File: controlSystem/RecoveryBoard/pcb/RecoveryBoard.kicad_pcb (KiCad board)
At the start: 2 copper layers, 102.7 x 56.8 mm, 150 parts, among them J1 Conn_01x06, J10 Conn_01x02, J11 Conn_01x03, J2 Thermistor, J3 Conn_01x04, J4 J-TE-Debug-2-1734592-0, J5 Conn_01x03, J6 Sensor Board 1, J7 Sensor Board 2, J8 Conn_01x06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

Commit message: Added rocket ready connector to ERS board
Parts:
- added J12: Conn_01x02, Connector_Molex:Molex_KK-254_AE-6410-02A_1x02_P2.54mm_Vertical, F.Cu at (119.8, 123.8)
- D8, D9: value D_Small -> SS210A
- moved TP24 5.53 mm to (122.1, 118.7)
- moved TP25 5.53 mm to (122.1, 116.9)
- moved TP26 2.90 mm to (122.1, 115.1)
- moved TP27 2.90 mm to (122.1, 113.3)
- moved TP8 2.90 mm to (122.1, 111.5)
- moved TP47 2.90 mm to (122.1, 109.7)
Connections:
- net Net-(TP41-Pad1) renamed /Microcontroller/ROCKET_READY
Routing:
- net /Microcontroller/USART2_TX: track 120.9 -> 243.6 mm, vias 2 -> 3
- net /Microcontroller/HALL2: track 119.6 -> 0.00 mm
- net /Microcontroller/ROCKET_READY: track 10.8 -> 22.6 mm
- net /Microcontroller/USART2_RX: track 114.7 -> 118.9 mm, vias 2 -> 3
- net BATT_READ: track 40.1 -> 43.4 mm
- net UMB_~{ON}: track 64.2 -> 66.5 mm
- net /Microcontroller/ISO_MAIN: track 16.8 -> 18.5 mm
- net MOTOR_ILIM: track 23.7 -> 22.7 mm
- net /Microcontroller/ISO_DROGUE: track 20.2 -> 21.3 mm
- net +3.3V: track 173.0 -> 172.3 mm
- net VBUS: vias 5 -> 0
- net GND: vias 56 -> 52
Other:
- board text added: "ROCKET READY"

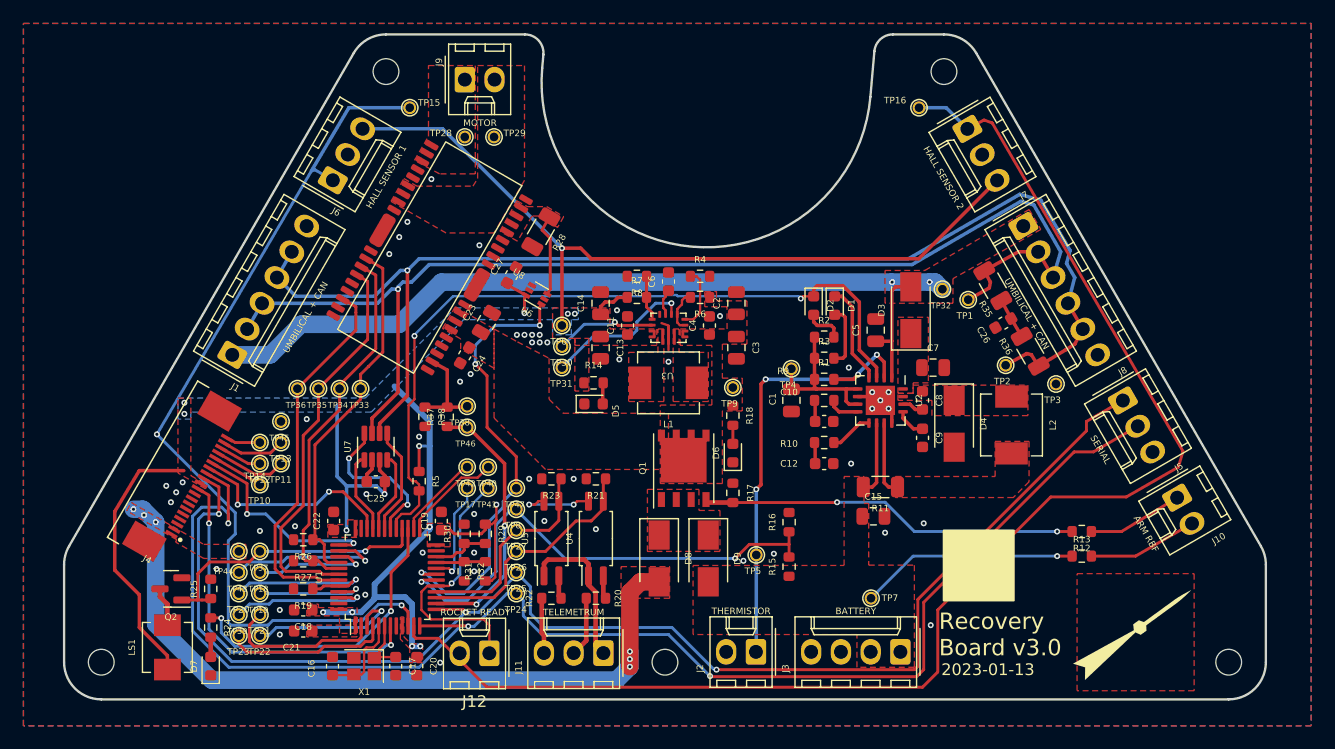
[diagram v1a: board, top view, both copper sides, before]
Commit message: Design review changes and cleaned up board layout.
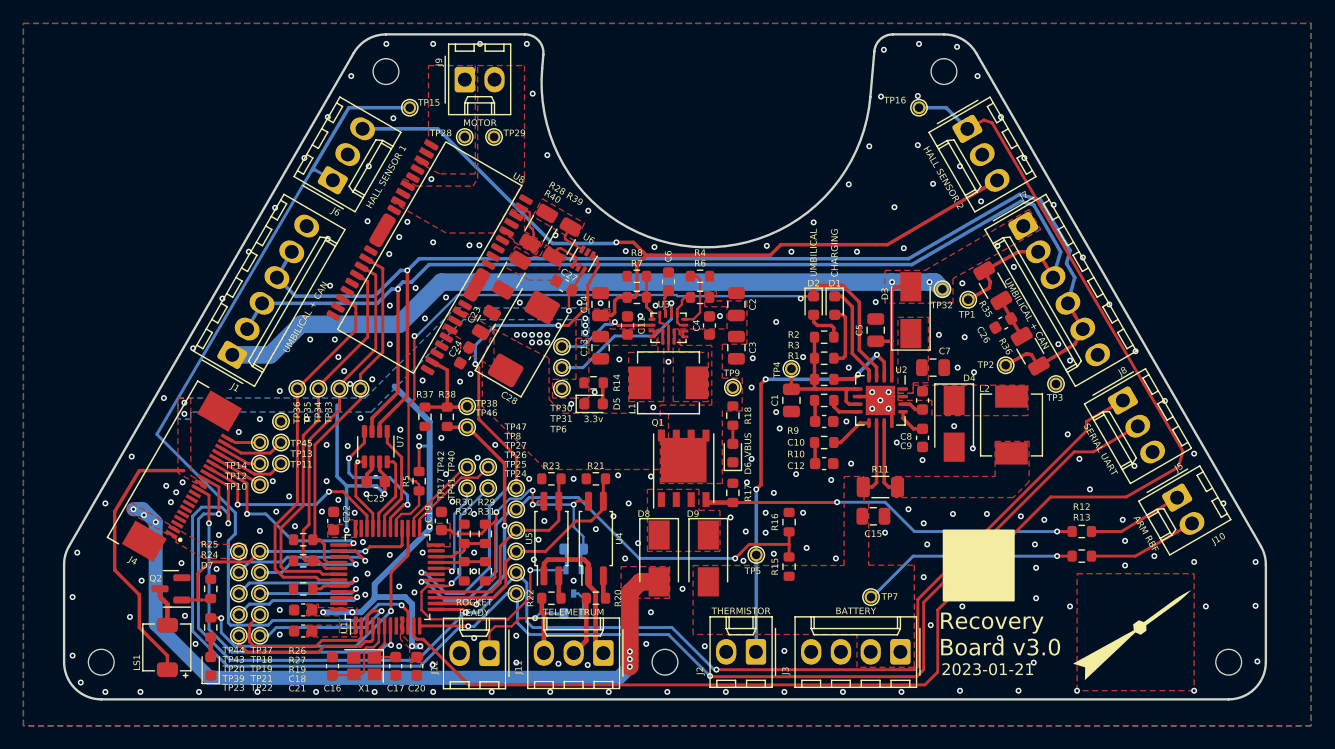
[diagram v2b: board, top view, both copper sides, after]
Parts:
- added C28: 100u, Capacitor_Tantalum_SMD:CP_EIA-7343-43_Kemet-X, F.Cu at (122.8, 97.0)
- added Q3: PMF170XP, Package_TO_SOT_SMD:SOT-323_SC-70, B.Cu at (127.0, 117.7)
- added R33: 10k, Resistor_SMD:R_0603_1608Metric, B.Cu at (127.0, 114.9)
- added R34: 10, Resistor_SMD:R_0603_1608Metric, B.Cu at (127.0, 120.4)
- added R39: 33m, Resistor_SMD:R_1206_3216Metric, F.Cu at (126.0, 88.7)
- added R40: 33m, Resistor_SMD:R_1206_3216Metric, F.Cu at (121.7, 91.5)
- C10: value 100n -> 2.2n
- D4: value 1N4007 -> SS210A
- LS1: footprint Inductor_SMD:L_Vishay_IHLP-1616 -> psas-footprints:SMT-0440-S-R
- R28: value Rsns -> 33m
- U7: footprint Package_TO_SOT_SMD:SOT-23-8 -> psas-footprints:SOT23-8
- moved TP6 5.40 mm to (126.0, 101.2)
- moved U6 4.95 mm to (127.8, 90.2), turned to -120 degrees
- moved C27 4.59 mm to (126.2, 92.4), turned to 150 degrees
- moved R28 0.36 mm to (124.0, 87.5), turned to 60 degrees
- moved C14 0.10 mm to (129.3, 94.0)
- moved C2 0.10 mm to (140.9, 94.0)
- moved TP7 0.10 mm to (152.4, 119.0)
- turned U7 to 0 degrees
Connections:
- net /Microcontroller/SDWIO renamed /Microcontroller/SWDIO
- J12 pad 1: /Microcontroller/ROCKET_READY -> Net-(J12-Pad1)
- R28 pad 2: GND -> Net-(R28-Pad2)
- U6 pad 3: Net-(R28-Pad1) -> Net-(R28-Pad2)
- U6 pad 4: GND -> Net-(R39-Pad2)
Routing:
- net /Microcontroller/HALL2: track 0.00 -> 119.4 mm
- net /Microcontroller/USART2_TX: track 243.6 -> 124.5 mm
- net /Microcontroller/ROCKET_READY: track 22.6 -> 31.5 mm, vias 1 -> 2
- net Net-(J12-Pad1): track 0.00 -> 8.84 mm, vias 0 -> 1
- net MOTOR_ISENSE: track 38.2 -> 46.4 mm
- net +3.3V: track 172.3 -> 179.6 mm, vias 17 -> 19
- net Net-(R28-Pad1): track 7.11 -> 3.67 mm
- net Net-(R39-Pad2): track 0.00 -> 3.22 mm
- net Net-(R28-Pad2): track 0.00 -> 2.88 mm
- net Net-(Q3-Pad3): track 0.00 -> 2.28 mm
- net CANL: track 108.1 -> 107.1 mm
- net CANH: track 103.5 -> 102.7 mm
- net BATT_READ: track 43.4 -> 44.2 mm
- net GND: track 6.13 -> 6.82 mm, vias 52 -> 259
- net /Microcontroller/USART2_RX: track 118.9 -> 119.4 mm
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- added copper zone on F.Cu, net Net-(R28-Pad2)
- added copper zone on F.Cu, net Net-(R39-Pad2)
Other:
- board text added: "2023-01-21"
- board text added: "3.3v"
- board text added: "CHARGING"
- board text added: "SERIAL UART"
- board text added: "UMBILICAL"
- board text added: "VBUS"
- board text removed: "2023-01-13"
- board text removed: "SERIAL"

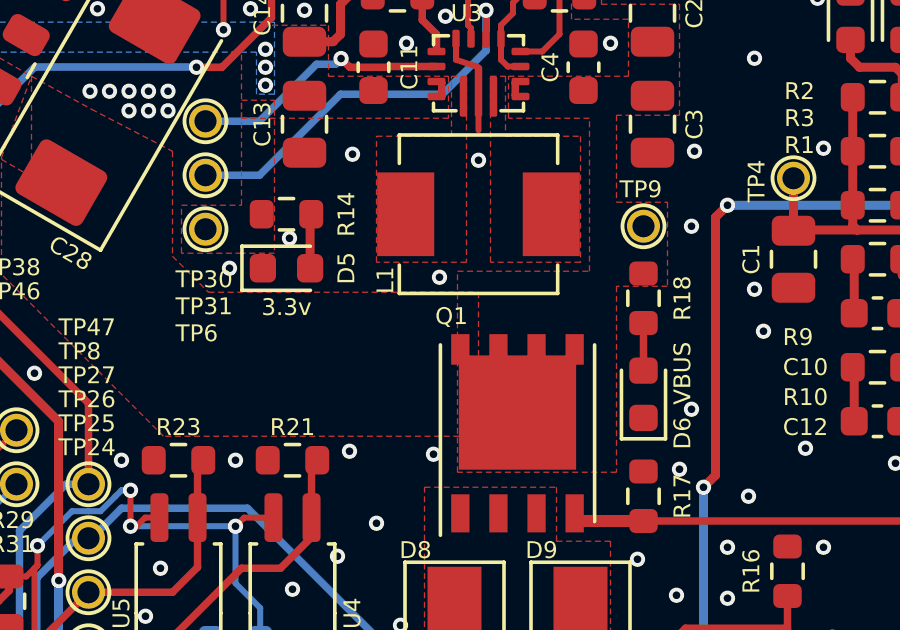
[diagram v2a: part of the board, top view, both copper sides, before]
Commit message: Updated ERS board stencil cutout for Q1
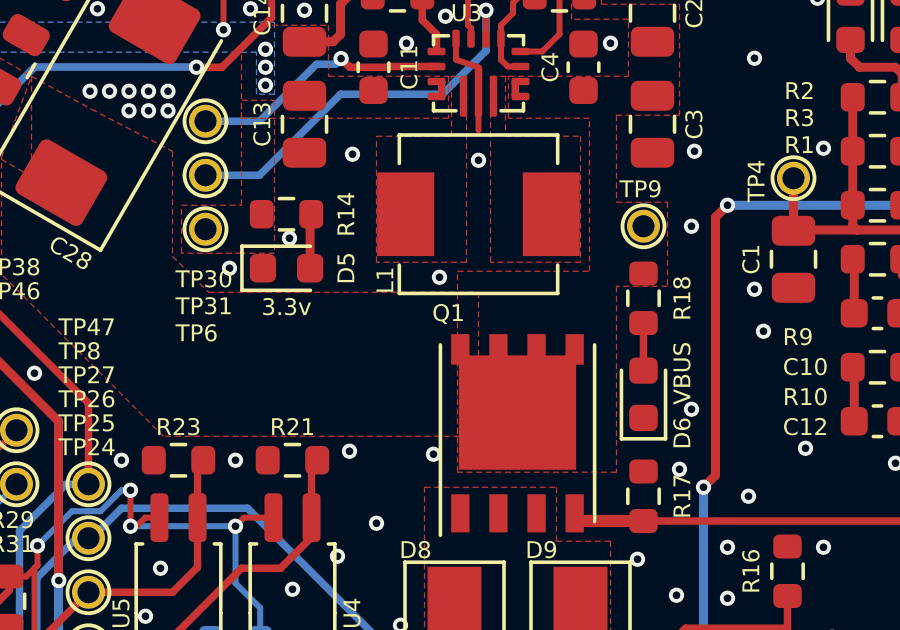
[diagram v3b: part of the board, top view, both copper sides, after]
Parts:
- D3, D4, D8, D9: value SS210A -> RBR5L30BDDTE25
- Q1: footprint Package_SO:PowerPAK_SO-8_Single -> psas-footprints:PowerPAK_SO-8_Single

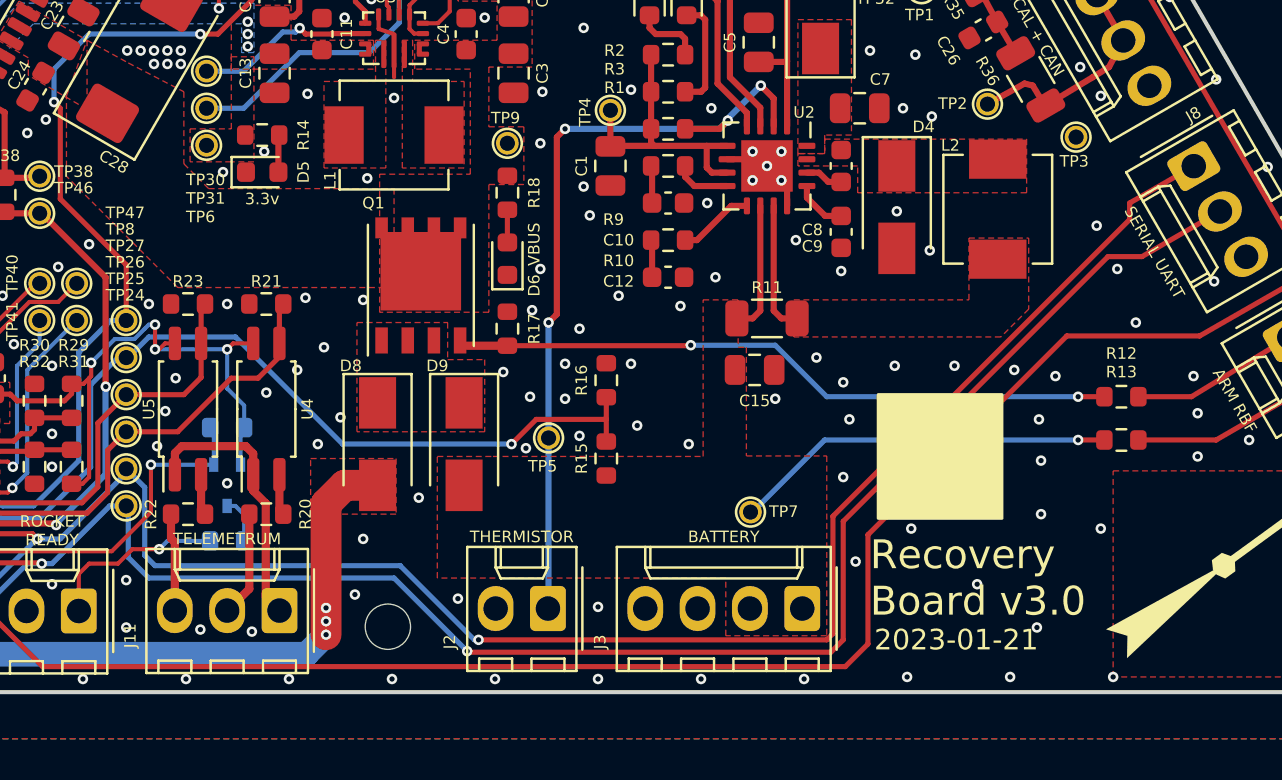
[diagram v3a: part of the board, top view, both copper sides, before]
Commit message: v3.1. Cap to deal with spikes on RBF, 100k on main Q pull down, better notes on schematic for part numbers, moved Vbatt pickoff to after main Q.
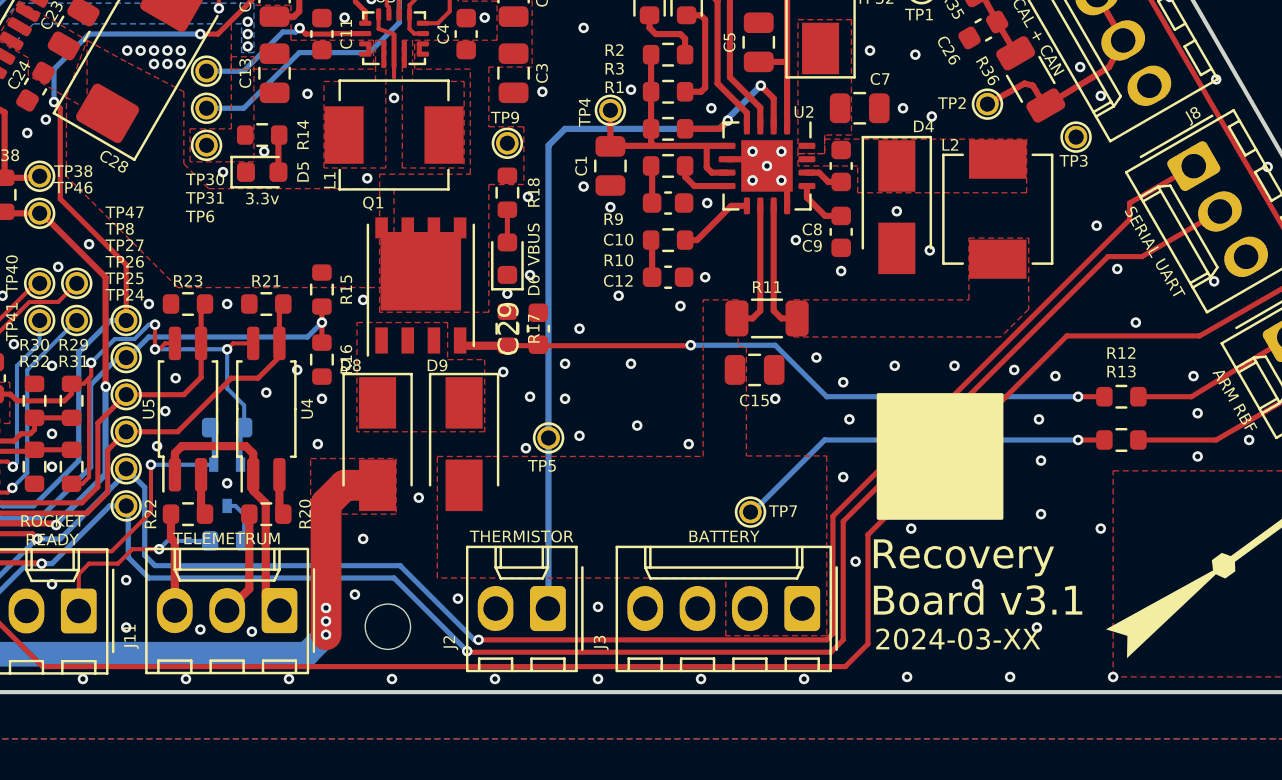
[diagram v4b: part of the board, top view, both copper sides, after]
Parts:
- added C29: 100n, Capacitor_SMD:C_0603_1608Metric, F.Cu at (142.1, 110.1)
- D7: value Green -> GRN
- J1, J8: value Conn_01x06 -> 00222-32051
- J10, J12: value Conn_01x02 -> 0022-232021
- J11, J5: value Conn_01x03 -> 0022-232031
- J3: value Conn_01x04 -> 0022-232041
- J6: value Sensor Board 1 -> 0022-232031
- J7: value Sensor Board 2 -> 0022-232031
- J9: value Motor -> 0022-232021
- R17: value 10k -> 100k
- U6: value INA185 -> INA185A1
- moved R15 16.1 mm to (131.6, 108.2), turned to -90 degrees
- moved R16 13.8 mm to (131.6, 111.6), turned to -90 degrees
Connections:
- net /Microcontroller/ROCKET_READY renamed /Microcontroller/~{ROCKET_READY}
- R15 pad 1: +BATT -> VBUS
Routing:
- net BATT_READ: track 44.2 -> 27.6 mm
- net Net-(J2-Pin_1): vias 4 -> 2
- net GND: vias 259 -> 257
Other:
- board text added: "2024-03-XX"
- board text added: "Recovery Board v3.1"
- board text removed: "2023-01-21"
- board text removed: "Recovery Board v3.0"

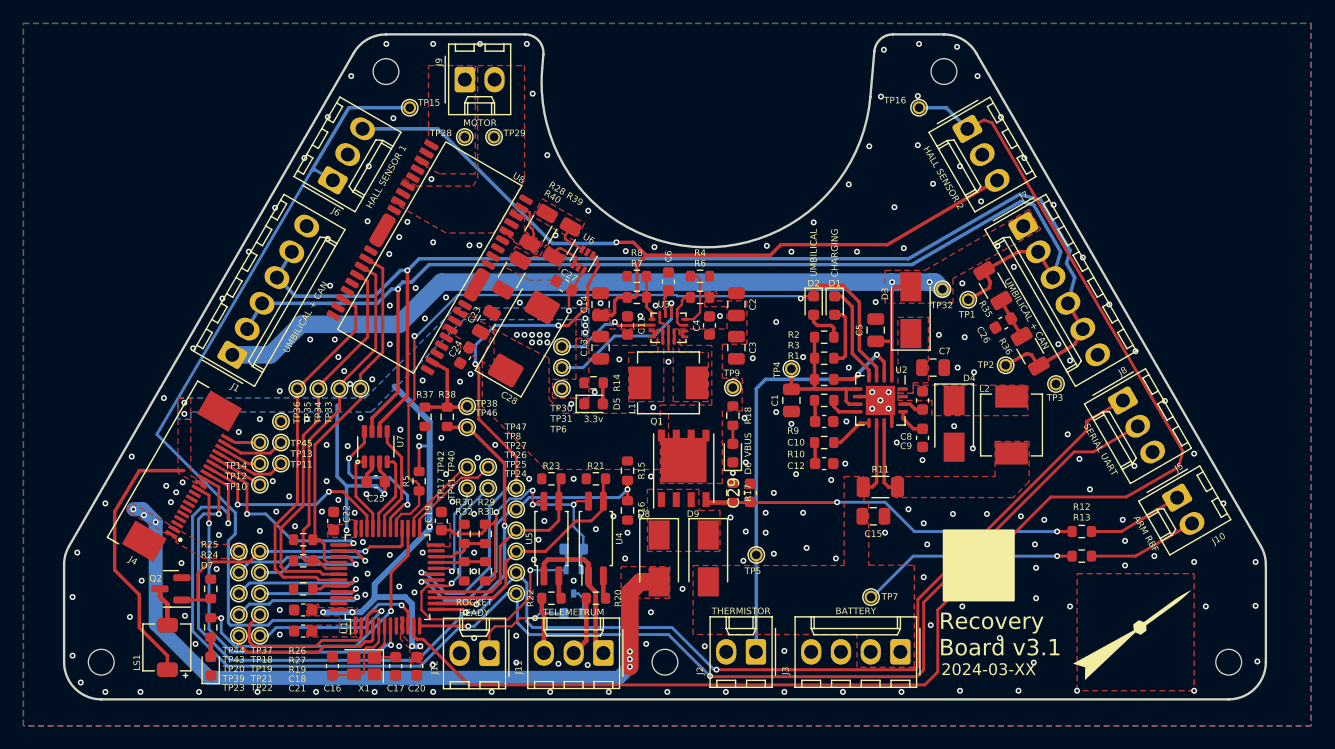
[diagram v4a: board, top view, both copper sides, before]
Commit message: Stuffing four more v3.0 PCBs and discovered everything wasn't updated. Fixed BOM, fixed a lot of schematic errors especially in symbols, fixed some footprint errors, synchronized schematic and pcb, and general cleanup. This board is still v3.1.
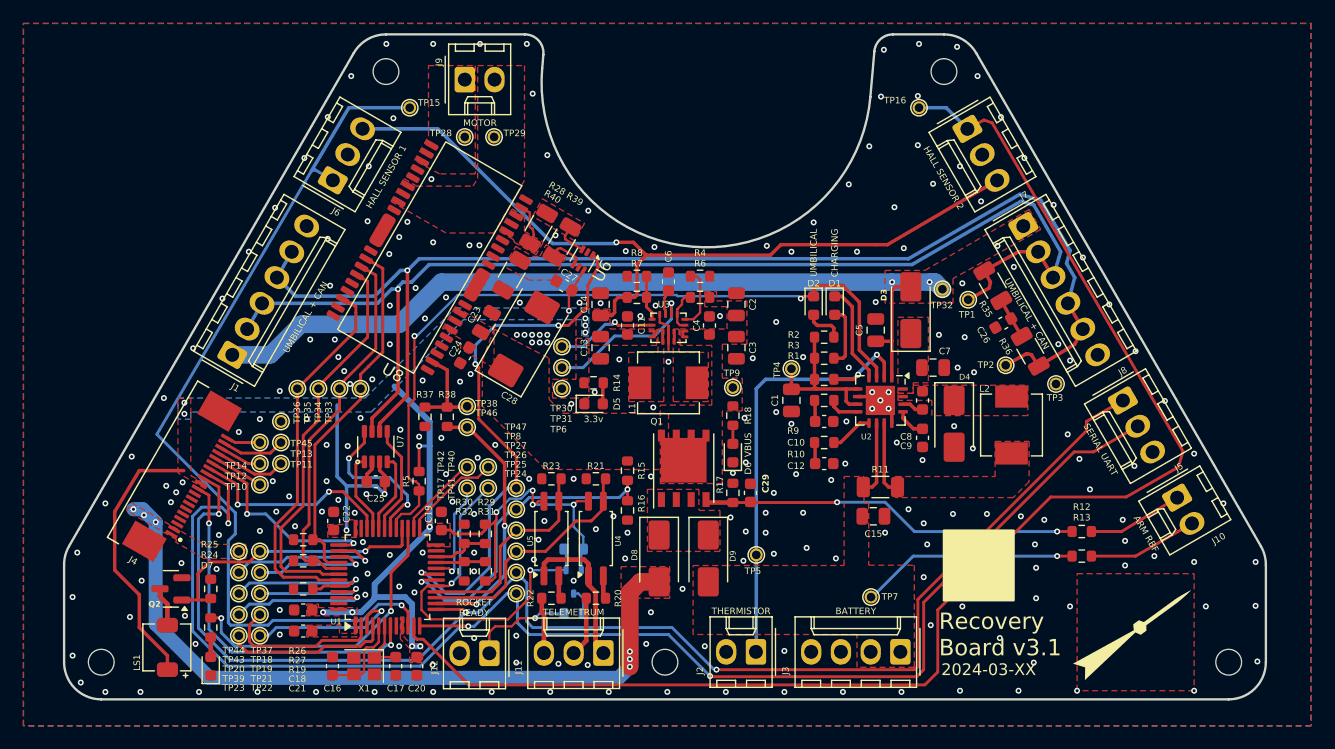
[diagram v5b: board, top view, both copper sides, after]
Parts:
- D1, D2, D5, D6: value Green -> GRN
- J2: value Thermistor -> 0022-232021
- R17: value 100k -> 150k
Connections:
- U8 pad 10: (no net) -> unconnected-(U8-Pad10)
- U8 pad 14: (no net) -> unconnected-(U8-Pad14)
- U8 pad 17: (no net) -> unconnected-(U8-Pad17)
- U8 pad 19: (no net) -> unconnected-(U8-Pad19)
- U8 pad 21: (no net) -> unconnected-(U8-Pad21)
- U8 pad 22: (no net) -> GND
- U8 pad 23: (no net) -> unconnected-(U8-Pad23)
- U8 pad 27: (no net) -> unconnected-(U8-Pad27)
- U8 pad 28: (no net) -> unconnected-(U8-Pad28)
- U8 pad 30: (no net) -> unconnected-(U8-Pad30)
- U8 pad 31: (no net) -> unconnected-(U8-Pad31)
- U8 pad 36: (no net) -> unconnected-(U8-Pad36)
- U8 pad 4: (no net) -> unconnected-(U8-Pad4)
- U8 pad 5: (no net) -> unconnected-(U8-Pad5)
- U8 pad 9: (no net) -> unconnected-(U8-Pad9)
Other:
- rule pad_to_mask_clearance: 0.0508 -> 0
